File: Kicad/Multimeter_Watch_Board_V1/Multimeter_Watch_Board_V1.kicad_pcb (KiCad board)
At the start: 4 copper layers, 5 parts, among them J1 AudioJack3_Ground_renamedPins, J2 AudioJack3_Ground_renamedPins, J3 AudioJack3_Ground_renamedPins, J4 Conn_01x16_Female, J5 Conn_01x16_Female

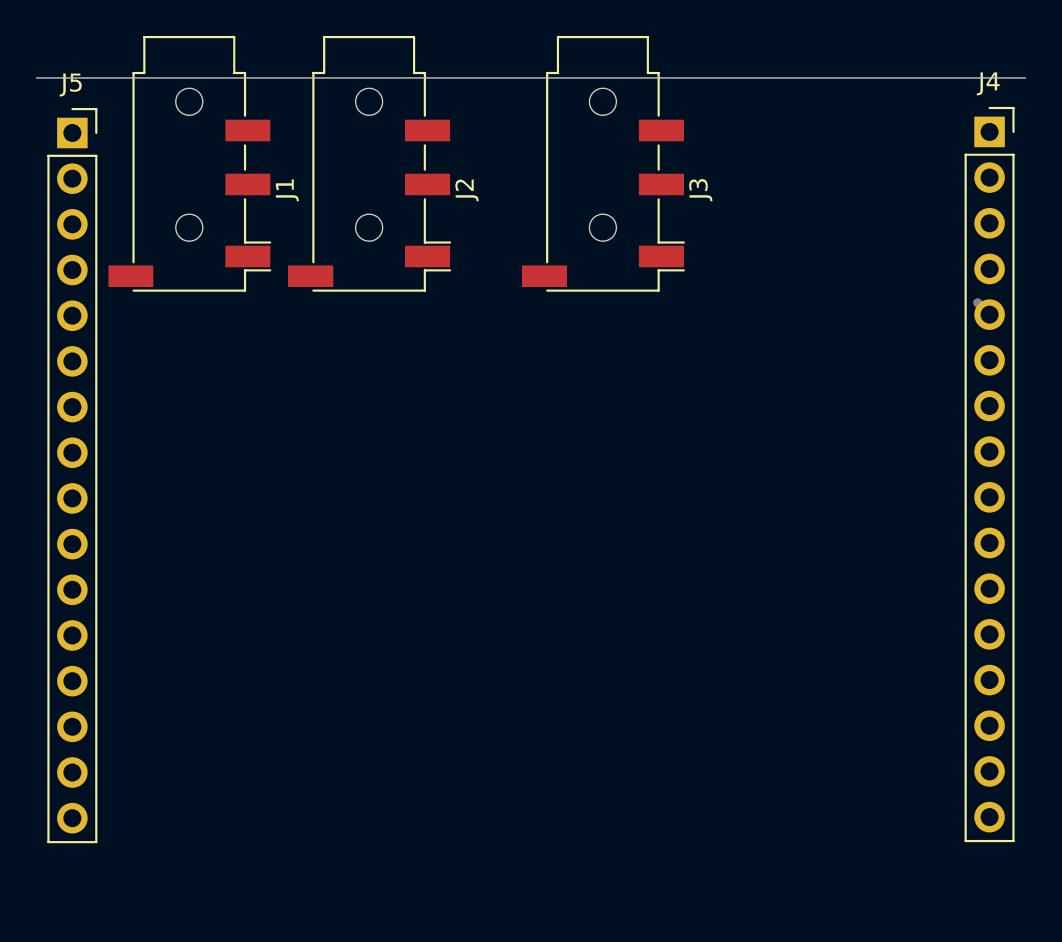
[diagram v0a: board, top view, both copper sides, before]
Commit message: second layout attempt, various pinout changes for better routing
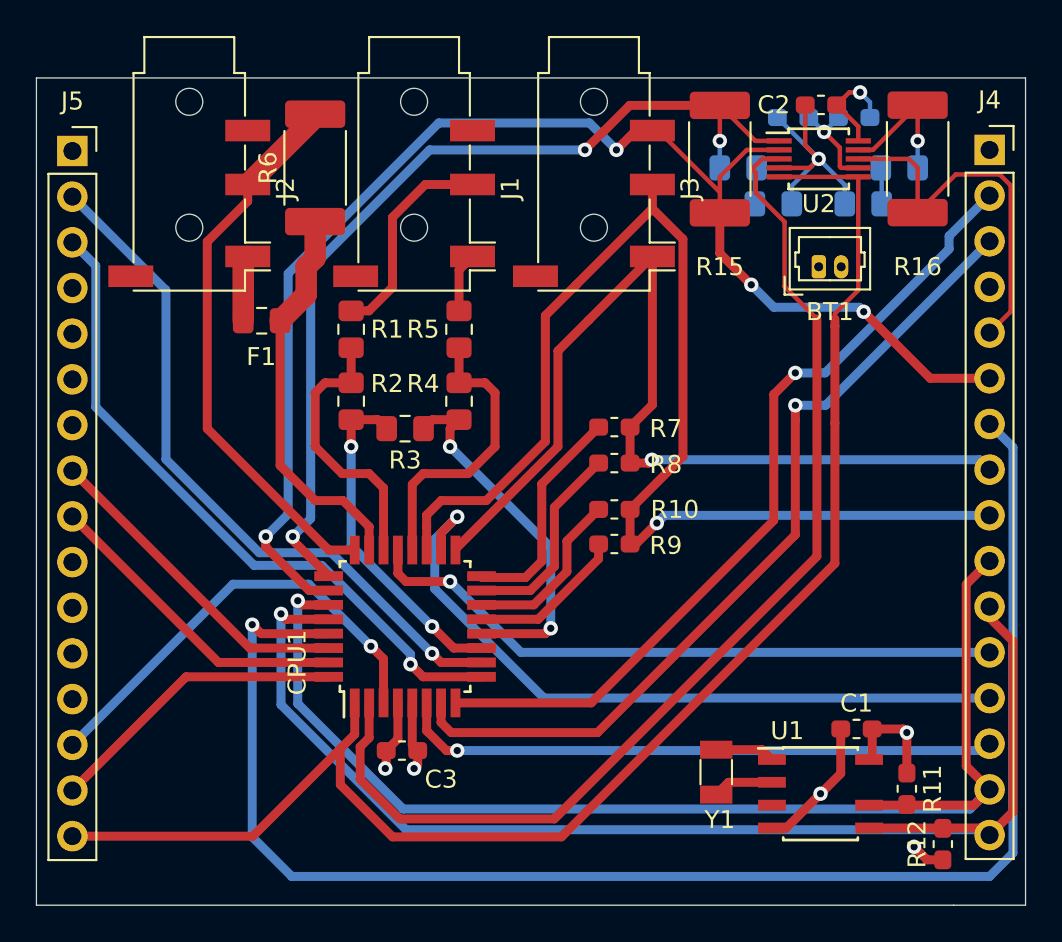
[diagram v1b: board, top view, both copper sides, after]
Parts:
- added BT1: Some Li-Po?, Connector_Molex:Molex_PicoBlade_53047-0210_1x02_P1.25mm_Vertical, F.Cu at (143.5, 60.5)
- added C1: 100n, Capacitor_SMD:C_0603_1608Metric_Pad1.05x0.95mm_HandSolder, F.Cu at (145.6, 86.2)
- added C2: 100n, Capacitor_SMD:C_0603_1608Metric_Pad1.05x0.95mm_HandSolder, F.Cu at (143.6, 51.5)
- added C3: 100n, Capacitor_SMD:C_0603_1608Metric_Pad1.05x0.95mm_HandSolder, F.Cu at (120.3, 87.4)
- added C4: C_Small, Capacitor_SMD:C_0805_2012Metric_Pad1.15x1.40mm_HandSolder, B.Cu at (141.0, 57.0)
- added C5: C_Small, Capacitor_SMD:C_0805_2012Metric_Pad1.15x1.40mm_HandSolder, B.Cu at (146.0, 57.0)
- added CPU1: LGT8F328P-QFP32L, Package_QFP:TQFP-32_7x7mm_P0.8mm, F.Cu at (120.5, 80.5)
- added F1: Fuse, Fuse:Fuse_0805_2012Metric_Pad1.15x1.40mm_HandSolder, F.Cu at (112.5, 63.5)
- added R1: R, Resistor_SMD:R_0805_2012Metric_Pad1.15x1.40mm_HandSolder, F.Cu at (117.5, 64.0)
- added R10: 680, Resistor_SMD:R_0603_1608Metric_Pad1.05x0.95mm_HandSolder, F.Cu at (132.1, 74.0)
- added R11: R, Resistor_SMD:R_0603_1608Metric_Pad1.05x0.95mm_HandSolder, F.Cu at (148.4, 89.5)
- added R12: R, Resistor_SMD:R_0603_1608Metric_Pad1.05x0.95mm_HandSolder, F.Cu at (150.4, 92.6)
- added R13: 1M, Resistor_SMD:R_0603_1608Metric_Pad1.05x0.95mm_HandSolder, B.Cu at (145.5, 52.2)
- added R14: 1M, Resistor_SMD:R_0603_1608Metric_Pad1.05x0.95mm_HandSolder, B.Cu at (142.1, 52.2)
- added R15: R, Resistor_SMD:R_2512_6332Metric_Pad1.52x3.35mm_HandSolder, F.Cu at (138.0, 54.5)
- added R16: 30, Resistor_SMD:R_2512_6332Metric_Pad1.52x3.35mm_HandSolder, F.Cu at (149.0, 54.5)
- added R17: R_Small, Resistor_SMD:R_0805_2012Metric_Pad1.15x1.40mm_HandSolder, B.Cu at (139.0, 55.0)
- added R18: R_Small, Resistor_SMD:R_0805_2012Metric_Pad1.15x1.40mm_HandSolder, B.Cu at (148.0, 55.0)
- added R2: R, Resistor_SMD:R_0805_2012Metric_Pad1.15x1.40mm_HandSolder, F.Cu at (117.5, 68.0)
- added R3: R, Resistor_SMD:R_0805_2012Metric_Pad1.15x1.40mm_HandSolder, F.Cu at (120.5, 69.5)
- added R4: R, Resistor_SMD:R_0805_2012Metric_Pad1.15x1.40mm_HandSolder, F.Cu at (123.5, 68.0)
- added R5: R, Resistor_SMD:R_0805_2012Metric_Pad1.15x1.40mm_HandSolder, F.Cu at (123.5, 64.0)
- added R6: R_shunt, Resistor_SMD:R_2512_6332Metric_Pad1.52x3.35mm_HandSolder, F.Cu at (115.5, 55.0)
- added R7: 470k, Resistor_SMD:R_0603_1608Metric_Pad1.05x0.95mm_HandSolder, F.Cu at (132.1, 69.4)
- added R8: 680, Resistor_SMD:R_0603_1608Metric_Pad1.05x0.95mm_HandSolder, F.Cu at (132.1, 71.4)
- added R9: 470k, Resistor_SMD:R_0603_1608Metric_Pad1.05x0.95mm_HandSolder, F.Cu at (132.1, 75.9)
- added U1: PCF85163-SO08, Package_SO:SOIC-8-N7_3.9x4.9mm_P1.27mm, F.Cu at (143.6, 89.8)
- added U2: AD8592, Package_SO:MSOP-10_3x3mm_P0.5mm, F.Cu at (143.5, 54.5)
- added Y1: 32kHz, Crystal:Crystal_SMD_3215-2Pin_3.2x1.5mm, F.Cu at (137.8, 88.6)
- moved J1 12.5 mm to (121.0, 56.1)
- moved J2 10.0 mm to (108.5, 56.1)
- moved J4 1.00 mm to (153.0, 54.0)
- moved J5 1.00 mm to (102.0, 54.1)
- moved J3 0.50 mm to (131.0, 56.1)
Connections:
- net /ADC2 renamed Net-(J2-Pad2)
- J2 pad 3: Net-(F1-Pad1) (its old number) -> /ADC1
- J3 pad 2: /ADC7 -> /ADC3
- J3 pad 4: /ADC1 -> /ADC11
- J4 pad 10: /SDA -> /SCL
- J4 pad 11: /SCL -> /SDA
- J4 pad 14: /BUTT3 -> /PE5
- J4 pad 15: /SDA -> /SCL
- J4 pad 16: /SCL -> /SDA
- J4 pad 2: /BUTT2 -> /PB7
- J4 pad 3: /BUTT1 -> /PB6
- J4 pad 6: /ADC1 -> /ADC3
- J4 pad 8: /ADC6 -> /ADC11
- J4 pad 9: /ADC7 -> /ADC6
- J5 pad 14: /BUTT6 -> /PE4
- J5 pad 15: /PB0 -> /PD2
- J5 pad 16: /PE4 -> /PD3
- J5 pad 2: /BUTT4 -> /PD6
- J5 pad 3: /BUTT5 -> /PD5
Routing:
- net /RESET: track 0.00 -> 84.4 mm, vias 0 -> 1
- net /PD3: track 0.00 -> 83.2 mm
- net /ADC3: track 0.00 -> 76.2 mm, vias 0 -> 4
- net /SDA: track 0.00 -> 70.9 mm, vias 0 -> 1
- net /SCL: track 0.00 -> 69.7 mm, vias 0 -> 1
- net /ADC6: track 0.00 -> 68.7 mm, vias 0 -> 1
- net /PD4: track 0.00 -> 61.6 mm
- net /ADC11: track 0.00 -> 53.2 mm, vias 0 -> 1
- net /ADC2: track 0.00 -> 52.4 mm, vias 0 -> 3
- net /PB6: track 0.00 -> 47.9 mm, vias 0 -> 1
- net /PB7: track 0.00 -> 46.5 mm, vias 0 -> 1
- net /SWC: track 0.00 -> 40.1 mm, vias 0 -> 1
- net /PD6: track 0.00 -> 39.0 mm, vias 0 -> 1
- net /PD5: track 0.00 -> 37.7 mm, vias 0 -> 1
- net /SWD: track 0.00 -> 36.0 mm, vias 0 -> 1
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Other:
- board outline added: 55 x 46 mm

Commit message: Kelvin connections for shunt; minor clearance improvements.
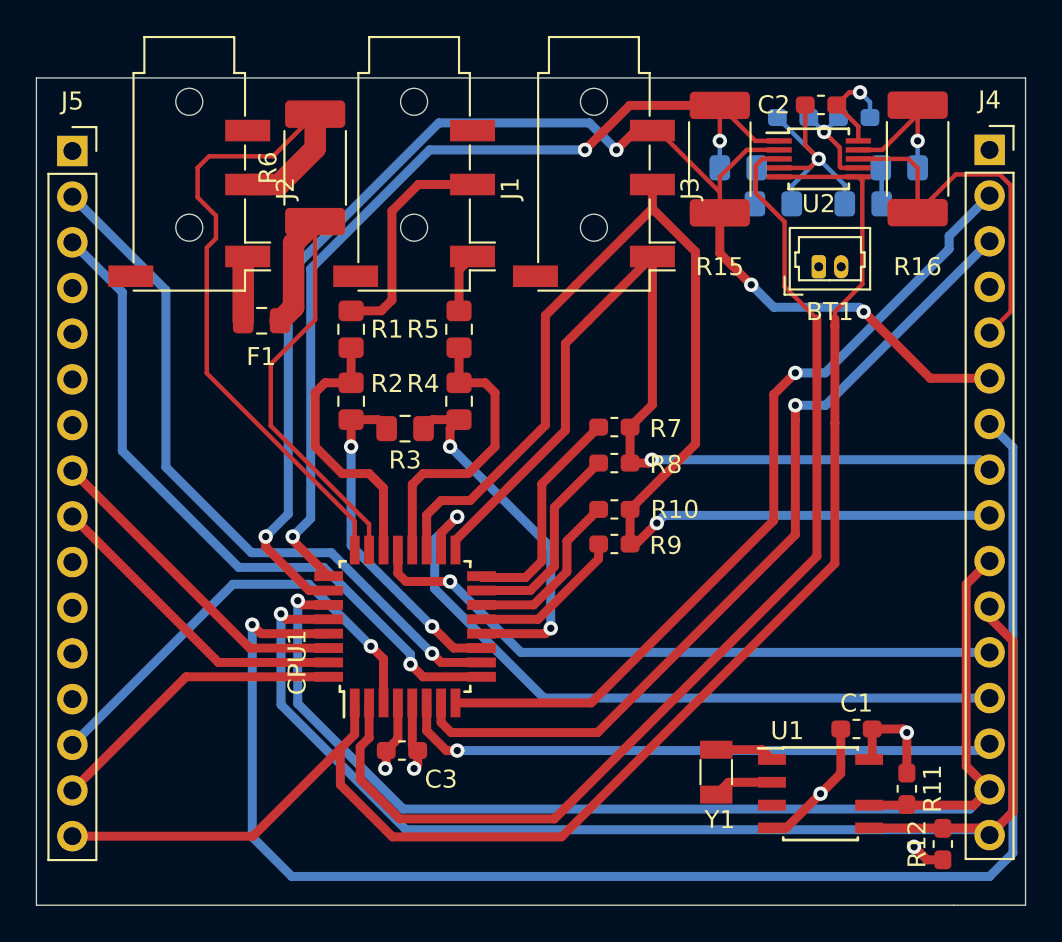
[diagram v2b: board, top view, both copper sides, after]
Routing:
- net /ADC1: track 31.0 -> 39.6 mm
- net /ADC0: track 22.0 -> 27.9 mm
- net Net-(J1-Pad3): track 11.9 -> 12.6 mm
- net /PD5: track 37.7 -> 38.3 mm

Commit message: add measurements, ensure headers are symmetrical
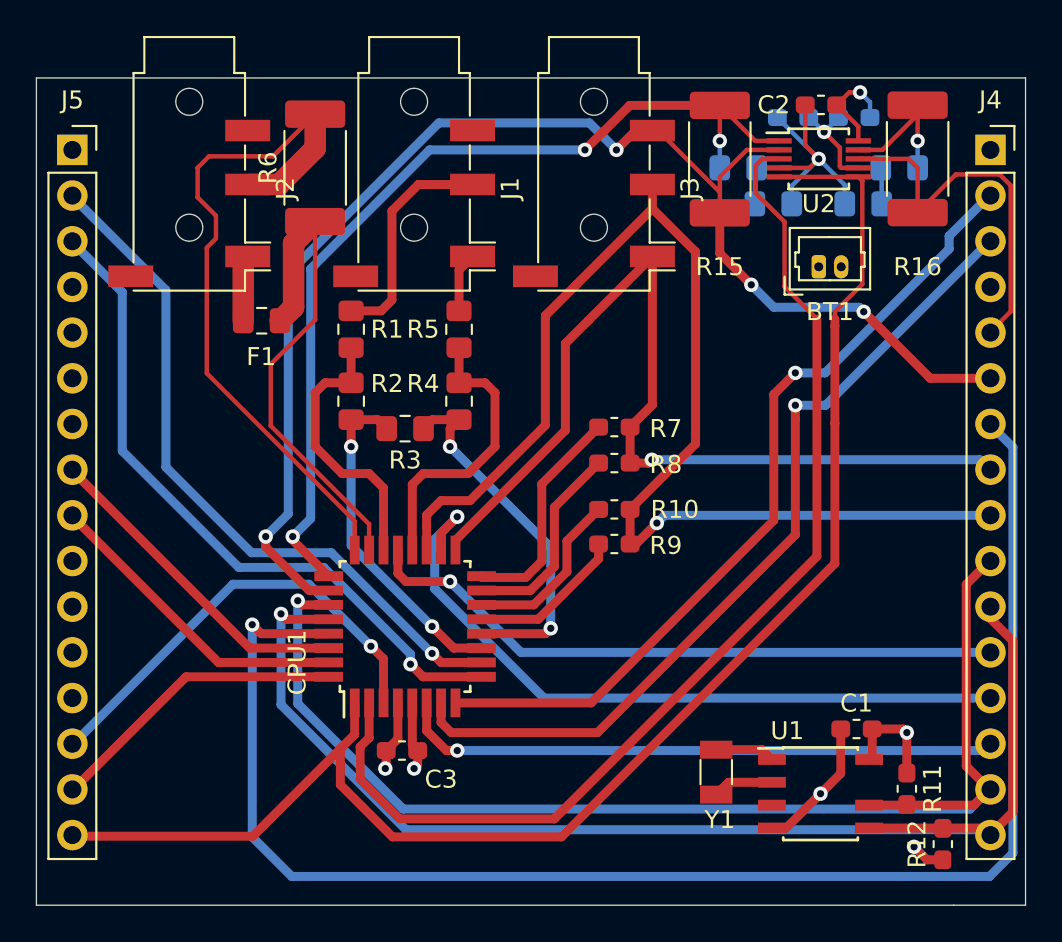
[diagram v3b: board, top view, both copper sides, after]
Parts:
- moved J5 0.06 mm to (102.0, 54.0)
- moved J4 0.05 mm to (153.1, 54.0)
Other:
- board text added: "Battery height"
- board text added: "Battery width"

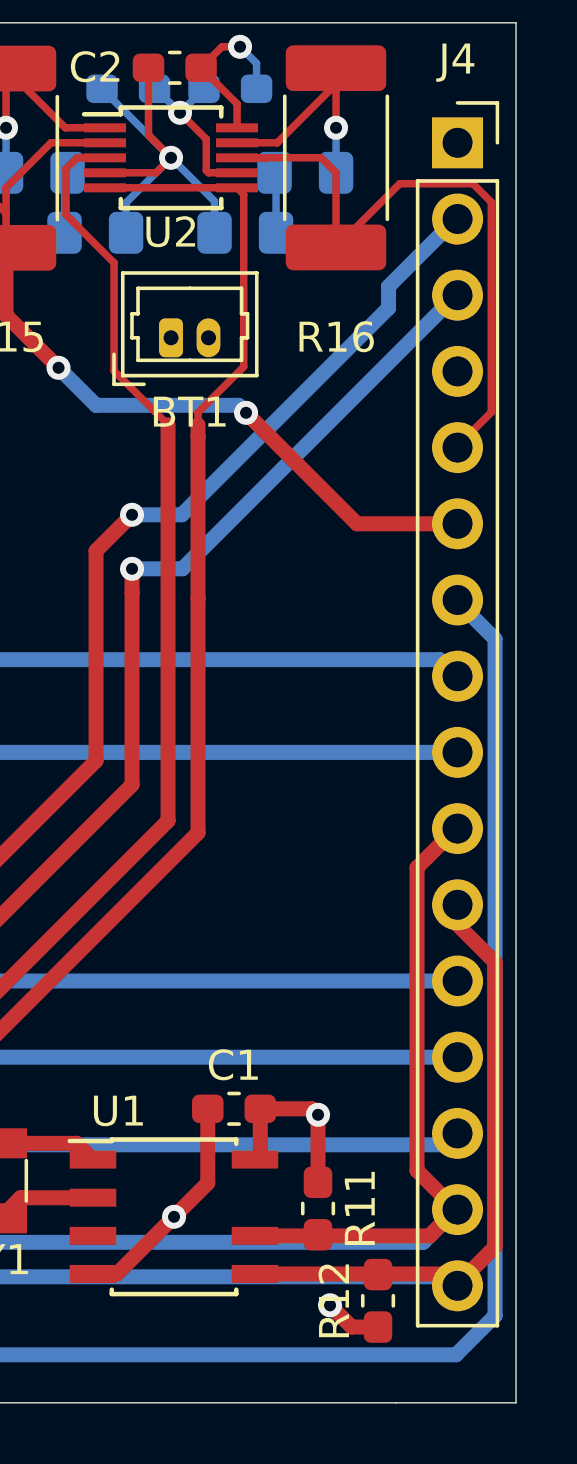
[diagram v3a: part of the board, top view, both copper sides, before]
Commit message: fix tracks too close after moving header
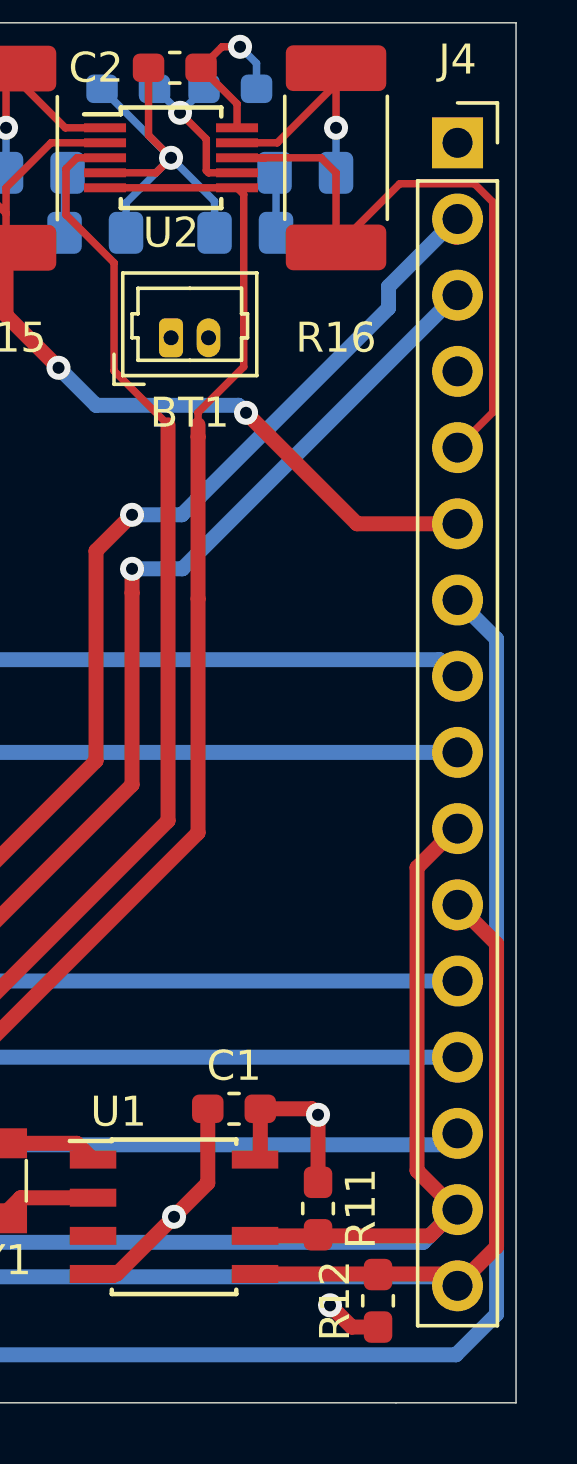
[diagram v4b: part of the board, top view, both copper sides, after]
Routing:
- net /SDA: track 70.9 -> 71.5 mm
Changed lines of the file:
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@@
   (segment (start 116.25 80.9) (end 112.5 80.9) (width 0.5) (layer F.Cu) (net 17))
   (segment (start 112.5 80.9) (end 112 80.4) (width 0.5) (layer F.Cu) (net 17))
-  (segment (start 154.300001 70.540001) (end 153 69.24) (width 0.5) (layer B.Cu) (net 17))
   (segment (start 112 80.4) (end 112 92.2) (width 0.5) (layer B.Cu) (net 17))
-  (segment (start 153 94.4) (end 154.300001 93.099999) (width 0.5) (layer B.Cu) (net 17))
   (segment (start 112 92.2) (end 114.2 94.4) (width 0.5) (layer B.Cu) (net 17))
-  (segment (start 154.300001 93.099999) (end 154.300001 70.540001) (width 0.5) (layer B.Cu) (net 17))
   (segment (start 114.2 94.4) (end 153 94.4) (width 0.5) (layer B.Cu) (net 17))
+  (segment (start 154.350001 93.049999) (end 154.350001 70.540001) (width 0.5) (layer B.Cu) (net 17))
+  (segment (start 154.350001 70.540001) (end 153.05 69.24) (width 0.5) (layer B.Cu) (net 17))
+  (segment (start 153 94.4) (end 154.350001 93.049999) (width 0.5) (layer B.Cu) (net 17))
   (via (at 113.6 79.8) (size 0.8) (drill 0.4) (layers F.Cu B.Cu) (net 18))
   (segment (start 116.25 80.1) (end 113.9 80.1) (width 0.5) (layer F.Cu) (net 18))
@@
   (segment (start 152.7 91.8) (end 153 92.1) (width 0.5) (layer B.Cu) (net 18))
   (segment (start 120.552036 91.8) (end 152.7 91.8) (width 0.5) (layer B.Cu) (net 18))
-  (segment (start 154.300001 90.799999) (end 153 92.1) (width 0.5) (layer F.Cu) (net 18))
-  (segment (start 154.300001 81.315999) (end 154.300001 90.799999) (width 0.5) (layer F.Cu) (net 18))
-  (segment (start 153 80.015998) (end 154.300001 81.315999) (width 0.5) (layer F.Cu) (net 18))
   (segment (start 153 79.4) (end 153 80.015998) (width 0.5) (layer F.Cu) (net 18))
   (segment (start 152.605 91.705) (end 153 92.1) (width 0.5) (layer F.Cu) (net 18))
   (segment (start 146.3 91.705) (end 152.605 91.705) (width 0.5) (layer F.Cu) (net 18))
+  (segment (start 154.350001 80.700001) (end 153.05 79.4) (width 0.5) (layer F.Cu) (net 18))
+  (segment (start 154.350001 90.799999) (end 154.350001 80.700001) (width 0.5) (layer F.Cu) (net 18))
+  (segment (start 153.05 92.1) (end 154.350001 90.799999) (width 0.5) (layer F.Cu) (net 18))
   (via (at 114.531458 79.068542) (size 0.8) (drill 0.4) (layers F.Cu B.Cu) (net 19))
   (segment (start 116.25 79.3) (end 114.762916 79.3) (width 0.5) (layer F.Cu) (net 19))
@@
   (segment (start 111.5 63.5) (end 111.5 60.175) (width 1.2) (layer F.Cu) (net 30))
   (segment (start 149 56.85) (end 149 57.4875) (width 0.25) (layer F.Cu) (net 31))
-  (segment (start 154.175001 55.975999) (end 154.175001 62.984999) (width 0.25) (layer F.Cu) (net 31))
-  (segment (start 153.564001 55.364999) (end 154.175001 55.975999) (width 0.25) (layer F.Cu) (net 31))
-  (segment (start 154.175001 62.984999) (end 153 64.16) (width 0.25) (layer F.Cu) (net 31))
-  (segment (start 151.122501 55.364999) (end 153.564001 55.364999) (width 0.25) (layer F.Cu) (net 31))
-  (segment (start 149 57.4875) (end 151.122501 55.364999) (width 0.25) (layer F.Cu) (net 31))
   (segment (start 146.5 54.5) (end 148.5 54.5) (width 0.25) (layer F.Cu) (net 31))
   (segment (start 146.5 54.5) (end 146.65 54.5) (width 0.25) (layer F.Cu) (net 31))
@@
   (segment (start 148.5 54.5) (end 149 55) (width 0.25) (layer F.Cu) (net 31))
   (segment (start 149 55) (end 149 57.4875) (width 0.25) (layer F.Cu) (net 31))
+  (segment (start 154.225001 62.984999) (end 153.05 64.16) (width 0.25) (layer F.Cu) (net 31))
+  (segment (start 154.225001 55.975999) (end 154.225001 62.984999) (width 0.25) (layer F.Cu) (net 31))
+  (segment (start 153.614001 55.364999) (end 154.225001 55.975999) (width 0.25) (layer F.Cu) (net 31))
+  (segment (start 151.122501 55.364999) (end 153.614001 55.364999) (width 0.25) (layer F.Cu) (net 31))
+  (segment (start 149 57.4875) (end 151.122501 55.364999) (width 0.25) (layer F.Cu) (net 31))
   (via (at 149 53.5) (size 0.8) (drill 0.4) (layers F.Cu B.Cu) (net 32))
   (segment (start 149 51.5125) (end 149 53.5) (width 0.25) (layer F.Cu) (net 32))
